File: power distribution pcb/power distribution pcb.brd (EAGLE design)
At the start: 30 parts, among them IC1 SN75176ASOIC, IC2 SN75176ASOIC, IC3 SN75176ASOIC, IC4 SN75176ASOIC, IC5 SN75176ASOIC, IC6 SN75176ASOIC

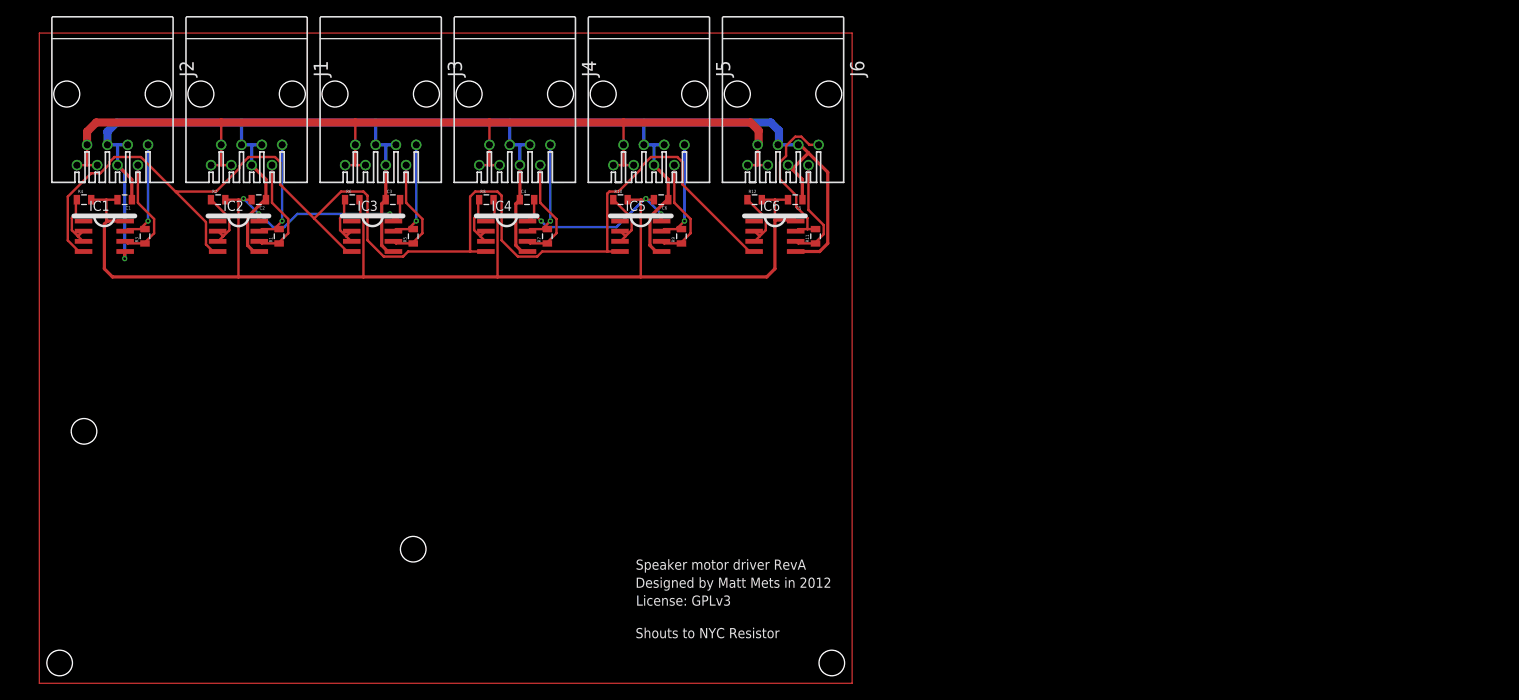
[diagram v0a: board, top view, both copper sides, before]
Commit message: Add design files for power distribution board
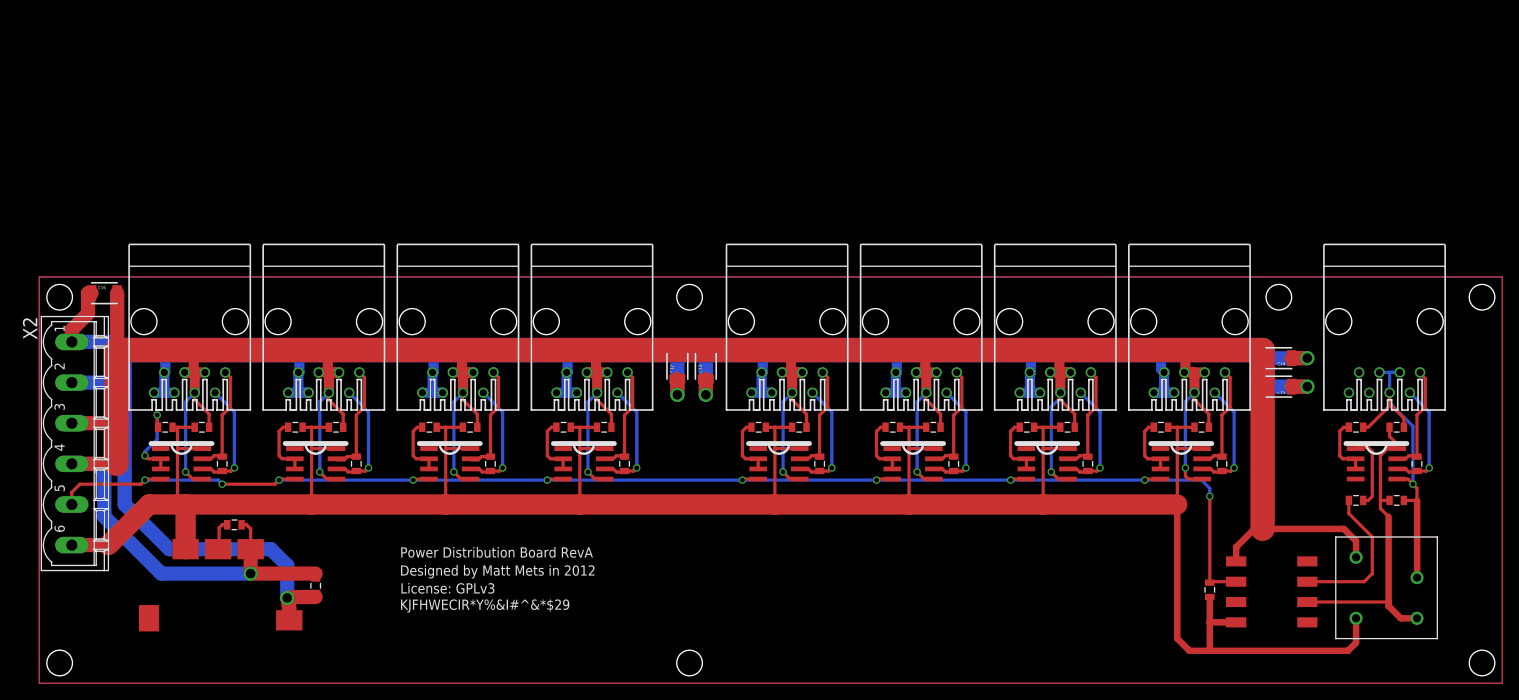
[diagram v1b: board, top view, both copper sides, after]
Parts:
- added C10, C11: ?F, SparkFun:0805
- added C12, C13, C14, C15, C16: (no value), SparkFun:1210
- added C7, C8, C9: 100nF, SparkFun:0805
- added IC7, IC8, IC9: SN75176ASOIC, reprap:SO08
- added J7, J8, J9: (no value), con-amp:520426-4
- added R13, R15, R17: 180, SparkFun:0805
- added R14, R16, R18: 10k, SparkFun:0805
- added R19, R20: 470, SparkFun:0805
- added R21: 1.472k, SparkFun:0805
- added U$1: NME0505DC, sonos_library:NME0505DC
- added U$2: OKI-T/3-W40N-C, sonos_library:OKI-T/3-W40N-C
- added U$3: 6N137, sonos_library:8_SOIC
- added X2: MSTBV6, con-phoenix-508:MSTBV6
- moved IC5 33.3 mm to (92.5, 27.4)
- moved IC6 33.3 mm to (109.2, 27.4)
- moved R9 33.3 mm to (97.5, 27.4)
- moved C5 33.3 mm to (111.8, 32.0)
- moved R11 33.3 mm to (114.3, 27.4)
- moved R12 33.3 mm to (106.7, 32.0)
- moved C6 33.3 mm to (95.0, 32.0)
- moved J6 33.3 mm to (110.2, 45.2)
- moved R10 33.3 mm to (89.9, 32.0)
- moved J5 33.3 mm to (93.5, 45.2)
- moved R4 30.2 mm to (15.7, 32.0)
- moved IC1 30.0 mm to (17.8, 27.4)
- moved IC2 30.0 mm to (34.5, 27.4)
- moved IC3 30.0 mm to (51.3, 27.4)
- moved IC4 30.0 mm to (68.1, 27.4)
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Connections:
- new net 5V_ISO: C10.2, C9.2, IC9.8, U$1.P$5, U$3.P$2
- new net D7: IC7.2, IC7.3, R14.1
- new net D8: IC8.2, IC8.3, R16.1
- new net D9: IC9.2, IC9.3, R18.1
- new net GND_ISO: C10.1, C9.1, IC9.5, J9.3, J9.4, J9.5, R18.2, U$1.P$7
- new net N$1: R19.1, U$3.P$3
- new net N$3: IC9.1, R19.2
- new net N$9: R21.2, U$2.TRIM
- new net RS485A7: IC7.6, J7.2, R13.1
- new net RS485A8: IC8.6, J8.2, R15.1
- new net RS485A9: IC9.6, J9.2, R17.1
- new net RS485B7: IC7.7, J7.1, R13.2
- new net RS485B8: IC8.7, J8.1, R15.2
- new net RS485B9: IC9.7, J9.1, R17.2
- net GND: now also C11.1, C12.2, C13.2, C14.2, C15.2, C16.2, C7.1, C8.1, IC7.5, IC8.5, J7.3, J7.4, J7.5, J8.3, J8.4, J8.5, R21.1, U$1.P$1, U$2.GROUND, U$3.P$5, X2.3, X2.4
- net TX: now also IC7.4, IC8.4, R20.1, U$3.P$6, X2.5
- net VCC: now also C7.2, C8.2, IC7.8, IC8.8, R14.2, R16.2, R20.2, U$1.P$4, U$2.VOUT, U$3.P$8, X2.6
- net VMOT: now also C11.2, C12.1, C13.1, C14.1, C15.1, C16.1, J7.6, J7.7, J7.8, J8.6, J8.7, J8.8, U$2.VIN, X2.1, X2.2
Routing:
- net N$7: track 264.2 -> 934.7 mm
- net GND: track 223.1 -> 487.1 mm, vias 1 -> 9
- net VMOT: track 130.0 -> 323.6 mm, vias 0 -> 5
- net VCC: track 208.0 -> 326.9 mm, vias 6 -> 0
- net N$1: track 101.6 -> 18.9 mm
- net GND_ISO: track 0.00 -> 46.3 mm, vias 0 -> 1
- net 5V_ISO: track 0.00 -> 40.3 mm
- net RS485A8: track 0.00 -> 14.8 mm, vias 0 -> 1
- net RS485A9: track 0.00 -> 14.8 mm, vias 0 -> 1
- net RS485A7: track 0.00 -> 14.8 mm, vias 0 -> 1
- net TX: track 162.6 -> 176.6 mm, vias 0 -> 10
- net RS485B9: track 0.00 -> 13.9 mm
- net RS485B7: track 0.00 -> 13.9 mm
- net RS485B8: track 0.00 -> 13.9 mm
- net N$3: track 0.00 -> 9.29 mm
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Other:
- board text added: "KJFHWECIR*Y%&I#^&*$29"
- board text added: "Power Distribution Board RevA"
- board text removed: "Shouts to NYC Resistor"
- board text removed: "Speaker motor driver RevA"
